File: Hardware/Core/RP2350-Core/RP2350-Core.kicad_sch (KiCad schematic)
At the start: 0 parts

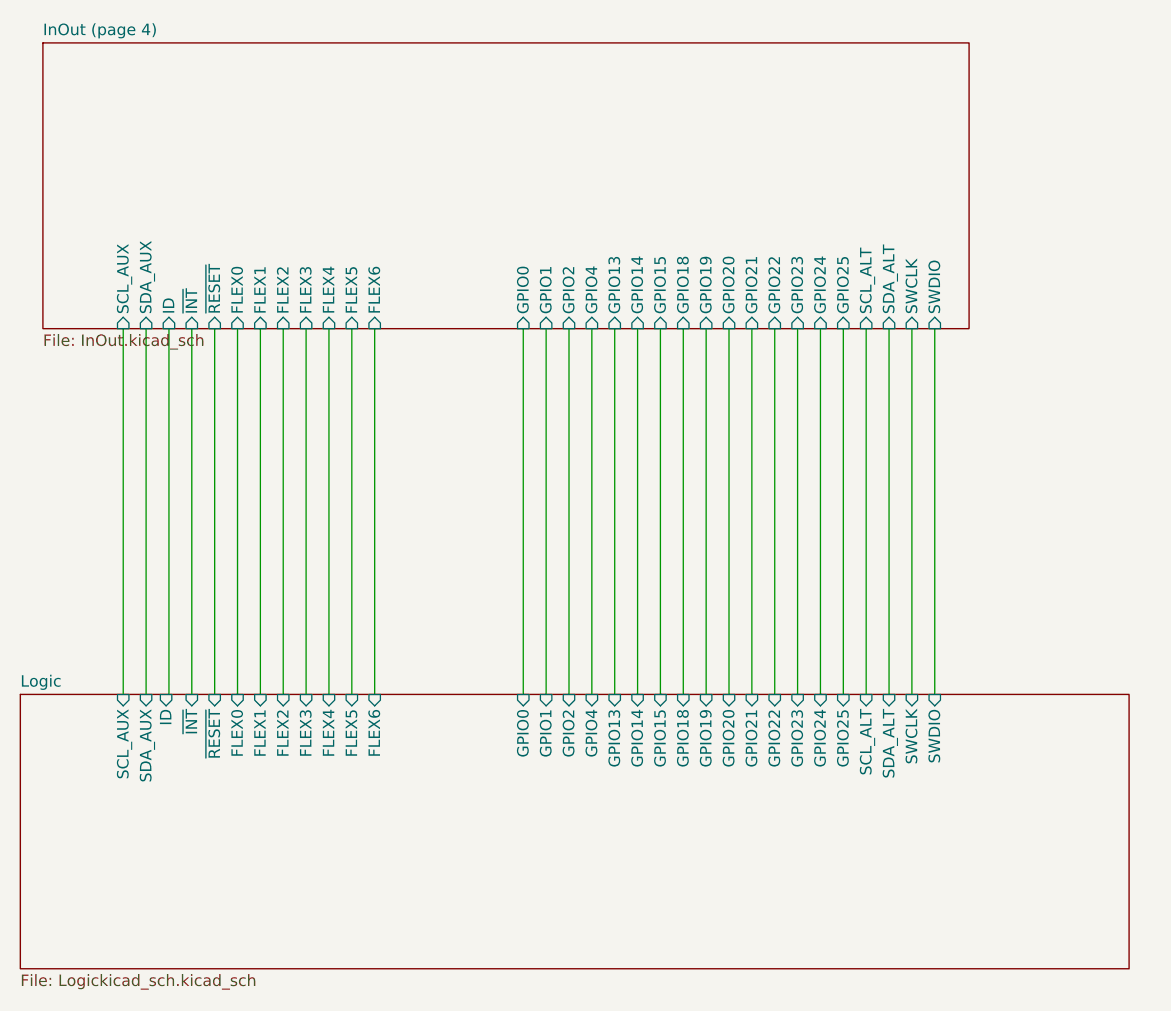
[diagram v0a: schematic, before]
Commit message: Placed footprints RP235x
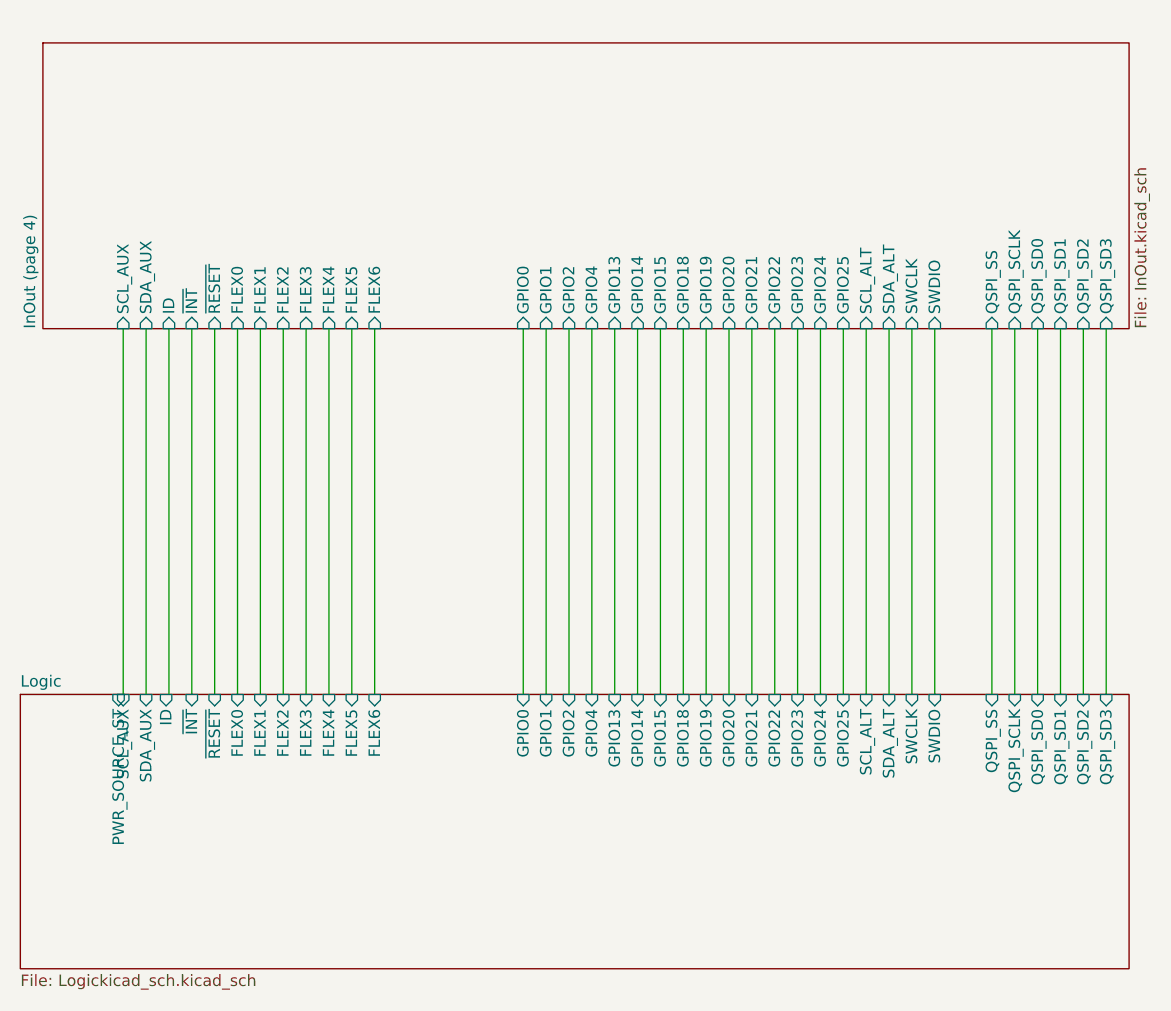
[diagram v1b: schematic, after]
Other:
- sheet InOut (page 4) ports: added QSPI_SCLK, QSPI_SD0, QSPI_SD1, QSPI_SD2, QSPI_SD3, QSPI_SS; removed none
- sheet Logic ports: added PWR_SOURCE_ST, QSPI_SCLK, QSPI_SD0, QSPI_SD1, QSPI_SD2, QSPI_SD3, QSPI_SS; removed none
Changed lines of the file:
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@@
+	(wire
+		(pts
+			(xy 232.41 57.15) (xy 232.41 97.79)
+		)
+		(stroke
+			(width 0)
+			(type default)
+		)
+	)
 	(wire
 		(pts
@@
 	(wire
 		(pts
+			(xy 234.95 57.15) (xy 234.95 97.79)
+		)
+		(stroke
+			(width 0)
+			(type default)
+		)
+	)
+	(wire
+		(pts
 			(xy 130.81 57.15) (xy 130.81 97.79)
 		)
@@
 	(wire
 		(pts
+			(xy 227.33 57.15) (xy 227.33 97.79)
+		)
+		(stroke
+			(width 0)
+			(type default)
+		)
+	)
+	(wire
+		(pts
 			(xy 185.42 57.15) (xy 185.42 97.79)
 		)
@@
 	(wire
 		(pts
+			(xy 240.03 57.15) (xy 240.03 97.79)
+		)
+		(stroke
+			(width 0)
+			(type default)
+		)
+	)
+	(wire
+		(pts
 			(xy 205.74 57.15) (xy 205.74 97.79)
 		)
@@
 	(wire
 		(pts
+			(xy 237.49 57.15) (xy 237.49 97.79)
+		)
+		(stroke
+			(width 0)
+			(type default)
+		)
+	)
+	(wire
+		(pts
 			(xy 140.97 57.15) (xy 140.97 97.79)
 		)
@@
 		(pts
 			(xy 175.26 57.15) (xy 175.26 97.79)
+		)
+		(stroke
+			(width 0)
+			(type default)
+		)
+	)
+	(wire
+		(pts
+			(xy 229.87 57.15) (xy 229.87 97.79)
 		)
 		(stroke
@@
 	(sheet
 		(at 121.8877 25.4)
-		(size 102.9023 31.75)
+		(size 120.6823 31.75)
 		(exclude_from_sim no)
 		(in_bom yes)
@@
 		)
 		(property "Sheetname" "InOut (page 4)"
-			(at 121.8877 24.6884 0)
+			(at 121.1761 57.15 90)
 			(show_name no)
 			(do_not_autoplace no)
@@
 		)
 		(property "Sheetfile" "InOut.kicad_sch"
-			(at 121.8877 57.7346 0)
+			(at 243.1546 57.15 90)
 			(show_name no)
 			(do_not_autoplace no)
@@
 		(pin "SWDIO" input
 			(at 220.98 57.15 270)
+			(effects
+				(font
+					(size 1.27 1.27)
+				)
+				(justify left)
+			)
+		)
+		(pin "QSPI_SD2" input
+			(at 237.49 57.15 270)
+			(effects
+				(font
+					(size 1.27 1.27)
+				)
+				(justify left)
+			)
+		)
+		(pin "QSPI_SD1" input
+			(at 234.95 57.15 270)
+			(effects
+				(font
+					(size 1.27 1.27)
+				)
+				(justify left)
+			)
+		)
+		(pin "QSPI_SD0" input
+			(at 232.41 57.15 270)
+			(effects
+				(font
+					(size 1.27 1.27)
+				)
+				(justify left)
+			)
+		)
+		(pin "QSPI_SD3" input
+			(at 240.03 57.15 270)
+			(effects
+				(font
+					(size 1.27 1.27)
+				)
+				(justify left)
+			)
+		)
+		(pin "QSPI_SCLK" input
+			(at 229.87 57.15 270)
+			(effects
+				(font
+					(size 1.27 1.27)
+				)
+				(justify left)
+			)
+		)
+		(pin "QSPI_SS" input
+			(at 227.33 57.15 270)
 			(effects
 				(font
@@
 			(effects
 				(font
+					(size 1.27 1.27)
+				)
+				(justify right)
+			)
+		)
+		(pin "QSPI_SD0" input
+			(at 232.41 97.79 90)
+			(effects
+				(font
+					(size 1.27 1.27)
+				)
+				(justify right)
+			)
+		)
+		(pin "QSPI_SCLK" input
+			(at 229.87 97.79 90)
+			(effects
+				(font
+					(size 1.27 1.27)
+				)
+				(justify right)
+			)
+		)
+		(pin "QSPI_SS" input
+			(at 227.33 97.79 90)
+			(effects
+				(font
+					(size 1.27 1.27)
+				)
+				(justify right)
+			)
+		)
+		(pin "QSPI_SD1" input
+			(at 234.95 97.79 90)
+			(effects
+				(font
+					(size 1.27 1.27)
+				)
+				(justify right)
+			)
+		)
+		(pin "QSPI_SD2" input
+			(at 237.49 97.79 90)
+			(effects
+				(font
+					(size 1.27 1.27)
+				)
+				(justify right)
+			)
+		)
+		(pin "QSPI_SD3" input
+			(at 240.03 97.79 90)
+			(effects
+				(font
+					(size 1.27 1.27)
+				)
+				(justify right)
+			)
+		)
+		(pin "PWR_SOURCE_ST" input
+			(at 130.2931 97.79 90)
+			(effects
+				(font

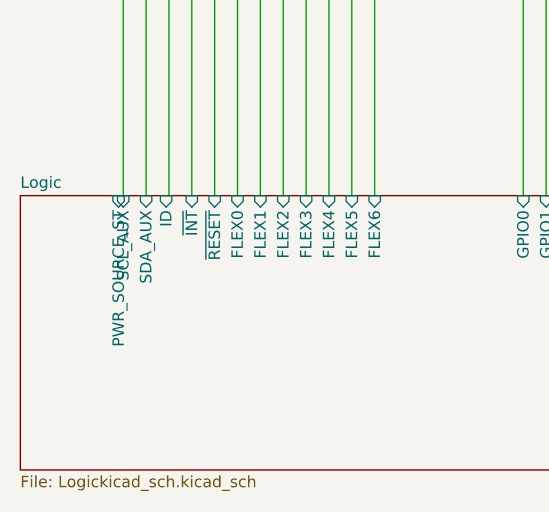
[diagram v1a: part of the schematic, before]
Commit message: Routing core started
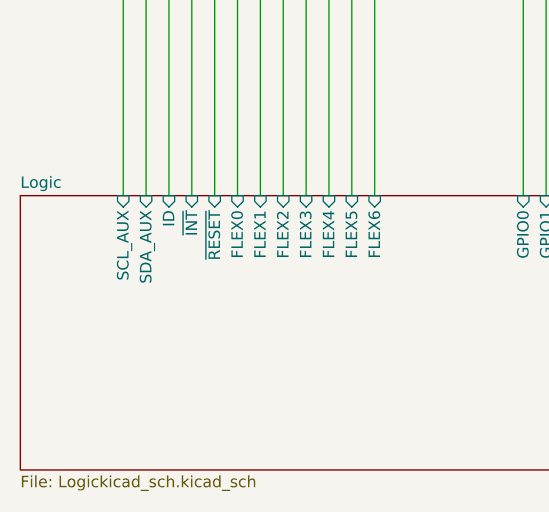
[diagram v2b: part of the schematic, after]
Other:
- sheet Logic ports: added none; removed PWR_SOURCE_ST
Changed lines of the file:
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@@
 		)
 		(pin "ID" input
-			(at 135.573 97.79 90)
+			(at 135.89 97.79 90)
 			(effects
 				(font
@@
 			(effects
 				(font
-					(size 1.27 1.27)
-				)
-				(justify right)
-			)
-		)
-		(pin "PWR_SOURCE_ST" input
-			(at 130.2931 97.79 90)
-			(effects
-				(font
